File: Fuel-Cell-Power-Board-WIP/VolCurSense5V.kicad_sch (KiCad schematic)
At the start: 11 parts, among them U5 ACS712xLCTR-05B, U8 TSV912IDT

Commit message: PCB started
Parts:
- U8: footprint (none) -> FPCB_Footprints:SO8_STM
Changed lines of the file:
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@@
           (reference "#PWR069") (unit 1)
         )
+        (path "/7aefa7f6-8562-49e0-9457-229f56bba97d/12238aff-aead-4dd2-8d1e-518f8d68aa91"
+          (reference "#PWR061") (unit 1)
+        )
       )
     )
@@
           (reference "R26") (unit 1)
         )
+        (path "/7aefa7f6-8562-49e0-9457-229f56bba97d/12238aff-aead-4dd2-8d1e-518f8d68aa91"
+          (reference "R7") (unit 1)
+        )
       )
     )
@@
           (reference "#PWR030") (unit 1)
         )
+        (path "/7aefa7f6-8562-49e0-9457-229f56bba97d/12238aff-aead-4dd2-8d1e-518f8d68aa91"
+          (reference "#PWR012") (unit 1)
+        )
       )
     )
@@
         (path "/7aefa7f6-8562-49e0-9457-229f56bba97d/59d9b0c4-d4f4-4be3-8a94-d2e2577f3ec5"
           (reference "#PWR070") (unit 1)
+        )
+        (path "/7aefa7f6-8562-49e0-9457-229f56bba97d/12238aff-aead-4dd2-8d1e-518f8d68aa91"
+          (reference "#PWR074") (unit 1)
         )
       )
@@
           (reference "R27") (unit 1)
         )
+        (path "/7aefa7f6-8562-49e0-9457-229f56bba97d/12238aff-aead-4dd2-8d1e-518f8d68aa91"
+          (reference "R9") (unit 1)
+        )
       )
     )
@@
           (reference "#PWR031") (unit 1)
         )
+        (path "/7aefa7f6-8562-49e0-9457-229f56bba97d/12238aff-aead-4dd2-8d1e-518f8d68aa91"
+          (reference "#PWR013") (unit 1)
+        )
       )
     )
@@
           (reference "C2") (unit 1)
         )
+        (path "/7aefa7f6-8562-49e0-9457-229f56bba97d/12238aff-aead-4dd2-8d1e-518f8d68aa91"
+          (reference "C18") (unit 1)
+        )
       )
     )
@@
           (reference "#PWR072") (unit 1)
         )
+        (path "/7aefa7f6-8562-49e0-9457-229f56bba97d/12238aff-aead-4dd2-8d1e-518f8d68aa91"
+          (reference "#PWR076") (unit 1)
+        )
       )
     )
@@
       (effects (font (size 1.27 1.27)) (justify left))
     )
-    (property "Footprint" "" (at 153.67 96.52 0)
+    (property "Footprint" "FPCB_Footprints:SO8_STM" (at 153.67 96.52 0)
       (effects (font (size 1.27 1.27)) hide)
     )
@@
           (reference "U10") (unit 3)
         )
+        (path "/7aefa7f6-8562-49e0-9457-229f56bba97d/12238aff-aead-4dd2-8d1e-518f8d68aa91"
+          (reference "U4") (unit 3)
+        )
       )
     )
@@
       (effects (font (size 1.27 1.27)))
     )
-    (property "Footprint" "" (at 138.43 55.88 0)
+    (property "Footprint" "FPCB_Footprints:SO8_STM" (at 138.43 55.88 0)
       (effects (font (size 1.27 1.27)) hide)
     )
@@
           (reference "U10") (unit 2)
         )
+        (path "/7aefa7f6-8562-49e0-9457-229f56bba97d/12238aff-aead-4dd2-8d1e-518f8d68aa91"
+          (reference "U4") (unit 2)
+        )
       )
     )
@@
           (reference "C3") (unit 1)
         )
+        (path "/7aefa7f6-8562-49e0-9457-229f56bba97d/12238aff-aead-4dd2-8d1e-518f8d68aa91"
+          (reference "C26") (unit 1)
+        )
       )
     )
@@
         (path "/7aefa7f6-8562-49e0-9457-229f56bba97d/59d9b0c4-d4f4-4be3-8a94-d2e2577f3ec5"
           (reference "R15") (unit 1)
+        )
+        (path "/7aefa7f6-8562-49e0-9457-229f56bba97d/12238aff-aead-4dd2-8d1e-518f8d68aa91"
+          (reference "R3") (unit 1)
         )
       )
@@
           (reference "U9") (unit 1)
         )
+        (path "/7aefa7f6-8562-49e0-9457-229f56bba97d/12238aff-aead-4dd2-8d1e-518f8d68aa91"
+          (reference "U1") (unit 1)
+        )
       )
     )
@@
         (path "/7aefa7f6-8562-49e0-9457-229f56bba97d/59d9b0c4-d4f4-4be3-8a94-d2e2577f3ec5"
           (reference "D9") (unit 1)
+        )
+        (path "/7aefa7f6-8562-49e0-9457-229f56bba97d/12238aff-aead-4dd2-8d1e-518f8d68aa91"
+          (reference "D17") (unit 1)
         )
       )
@@
       (effects (font (size 1.27 1.27)))
     )
-    (property "Footprint" "" (at 92.71 81.28 0)
+    (property "Footprint" "FPCB_Footprints:SO8_STM" (at 92.71 81.28 0)
       (effects (font (size 1.27 1.27)) hide)
     )
@@
           (reference "U10") (unit 1)
         )
+        (path "/7aefa7f6-8562-49e0-9457-229f56bba97d/12238aff-aead-4dd2-8d1e-518f8d68aa91"
+          (reference "U4") (unit 1)
+        )
       )
     )
@@
           (reference "C4") (unit 1)
         )
+        (path "/7aefa7f6-8562-49e0-9457-229f56bba97d/12238aff-aead-4dd2-8d1e-518f8d68aa91"
+          (reference "C20") (unit 1)
+        )
       )
     )
@@
           (reference "#PWR034") (unit 1)
         )
+        (path "/7aefa7f6-8562-49e0-9457-229f56bba97d/12238aff-aead-4dd2-8d1e-518f8d68aa91"
+          (reference "#PWR060") (unit 1)
+        )
       )
     )
@@
           (reference "#PWR071") (unit 1)
         )
+        (path "/7aefa7f6-8562-49e0-9457-229f56bba97d/12238aff-aead-4dd2-8d1e-518f8d68aa91"
+          (reference "#PWR075") (unit 1)
+        )
       )
     )
@@
           (reference "D13") (unit 1)
         )
+        (path "/7aefa7f6-8562-49e0-9457-229f56bba97d/12238aff-aead-4dd2-8d1e-518f8d68aa91"
+          (reference "D15") (unit 1)
+        )
       )
     )
@@
           (reference "#PWR033") (unit 1)
         )
+        (path "/7aefa7f6-8562-49e0-9457-229f56bba97d/12238aff-aead-4dd2-8d1e-518f8d68aa91"
+          (reference "#PWR059") (unit 1)
+        )
       )
     )
@@
           (reference "#PWR032") (unit 1)
         )
+        (path "/7aefa7f6-8562-49e0-9457-229f56bba97d/12238aff-aead-4dd2-8d1e-518f8d68aa91"
+          (reference "#PWR058") (unit 1)
+        )
       )
     )
@@
         (path "/7aefa7f6-8562-49e0-9457-229f56bba97d/59d9b0c4-d4f4-4be3-8a94-d2e2577f3ec5"
           (reference "#PWR073") (unit 1)
+        )
+        (path "/7aefa7f6-8562-49e0-9457-229f56bba97d/12238aff-aead-4dd2-8d1e-518f8d68aa91"
+          (reference "#PWR077") (unit 1)
         )
       )
@@
           (reference "R16") (unit 1)
         )
-      )
+        (path "/7aefa7f6-8562-49e0-9457-229f56bba97d/12238aff-aead-4dd2-8d1e-518f8d68aa91"
+          (reference "R5") (unit 1)
+        )
+      )

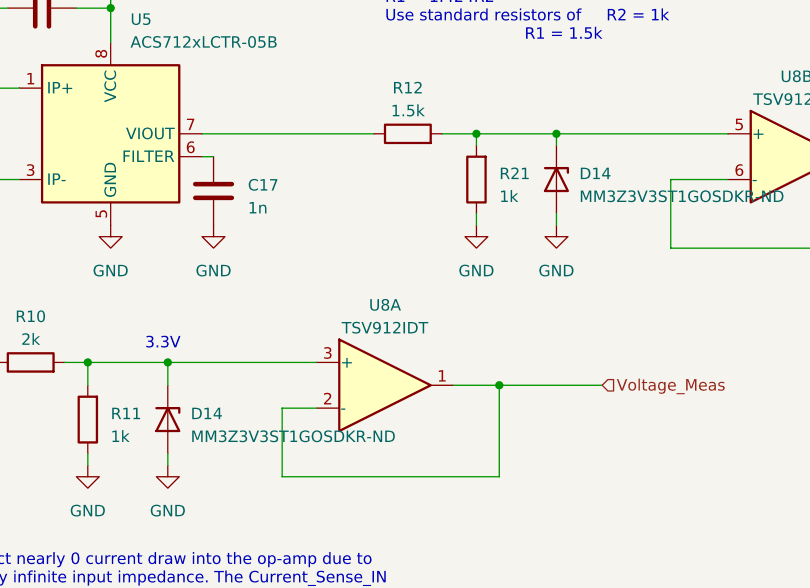
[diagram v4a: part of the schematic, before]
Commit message: Reworking the schematic and updating symbols with footprints. Added symbol & ftp library from the battery power board to aid in development
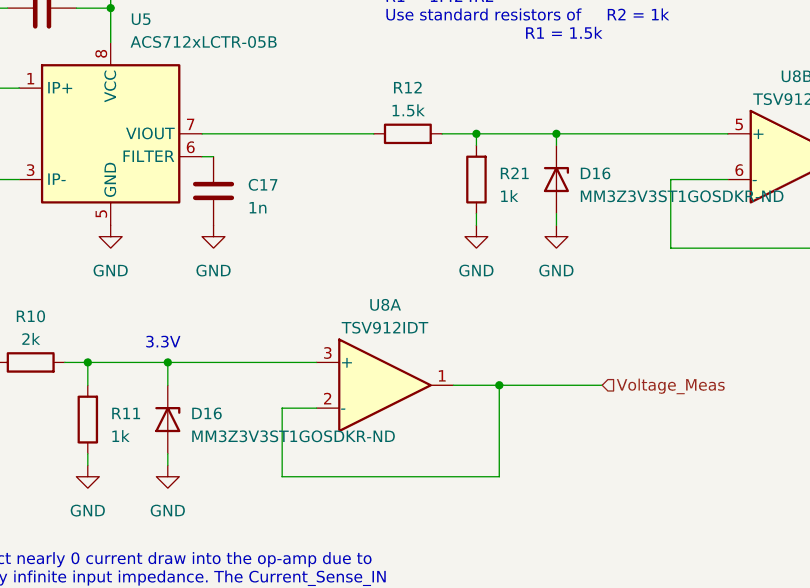
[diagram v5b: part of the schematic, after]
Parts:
- removed D14 (x2): MM3Z3V3ST1GOSDKR-ND, FPCB_Footprints:SOD-323_1P8X1P35_ONS, symbol Device:D_Zener
- added D16 (x2): MM3Z3V3ST1GOSDKR-ND, Diode_SMD:D_SOD-323, symbol Device:D_Zener
- U8: footprint FPCB_Footprints:SO8_STM -> BATT_FTP:SO8_STM
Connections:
- net GND: now also D16.2 (A), D16.2 (A)
- net at R12.2, R21.2, U8.5 (+): now also D16.1 (K)
- net at R10.2, R11.2, U8.3 (+): now also D16.1 (K)
